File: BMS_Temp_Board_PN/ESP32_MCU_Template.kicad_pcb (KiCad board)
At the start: 2 copper layers, 195.2 x 109.5 mm, 81 parts, among them IC1 ESP32-S3-WROOM-1-N8R8, IC10 CD74HC4067PWR, IC11 CD74HC4067PWR, IC12 CD74HC4067PWR, IC13 CD74HC4067PWR, IC14 CD74HC4067PWR, IC15 CD74HC4067PWR, IC16 CD74HC4067PWR, IC17 CD74HC4067PWR, IC18 CD74HC4067PWR, IC19 CD74HC4067PWR, IC2 CP2102N-A02-GQFN28, IC20 CD74HC4067PWR, IC21 CD74HC4067PWR, IC22 CD74HC4067PWR, IC23 CD74HC4067PWR, IC24 CD74HC4067PWR, IC3 TLP175A_TPL,E, IC4 TPS2116DRLR, IC5 MIC37100-3.3WS, IC6 CD74HC4067PWR, IC7 CD74HC4067PWR, IC8 CD74HC4067PWR, IC9 CD74HC4067PWR, J1 ESP_USB, J10 B32B-PUDSS-1_LF__SN_, J11 B32B-PUDSS-1_LF__SN_, J12 B32B-PUDSS-1_LF__SN_, J13 B32B-PUDSS-1_LF__SN_, J14 B32B-PUDSS-1_LF__SN_, J15 B32B-PUDSS-1_LF__SN_, J16 B32B-PUDSS-1_LF__SN_, J17 B32B-PUDSS-1_LF__SN_, J18 B32B-PUDSS-1_LF__SN_, J19 B32B-PUDSS-1_LF__SN_, J2 B32B-PUDSS-1_LF__SN_, J20 B32B-PUDSS-1_LF__SN_, J3 B32B-PUDSS-1_LF__SN_, J4 B32B-PUDSS-1_LF__SN_, J5 B32B-PUDSS-1_LF__SN_, J6 B32B-PUDSS-1_LF__SN_, J7 B32B-PUDSS-1_LF__SN_, J8 B32B-PUDSS-1_LF__SN_, J9 B32B-PUDSS-1_LF__SN_, Q1 MMBT2222LT1G, Q2 MMBT2222LT1G, U1 USBLC6-2SC6, U2 SN65HVD230

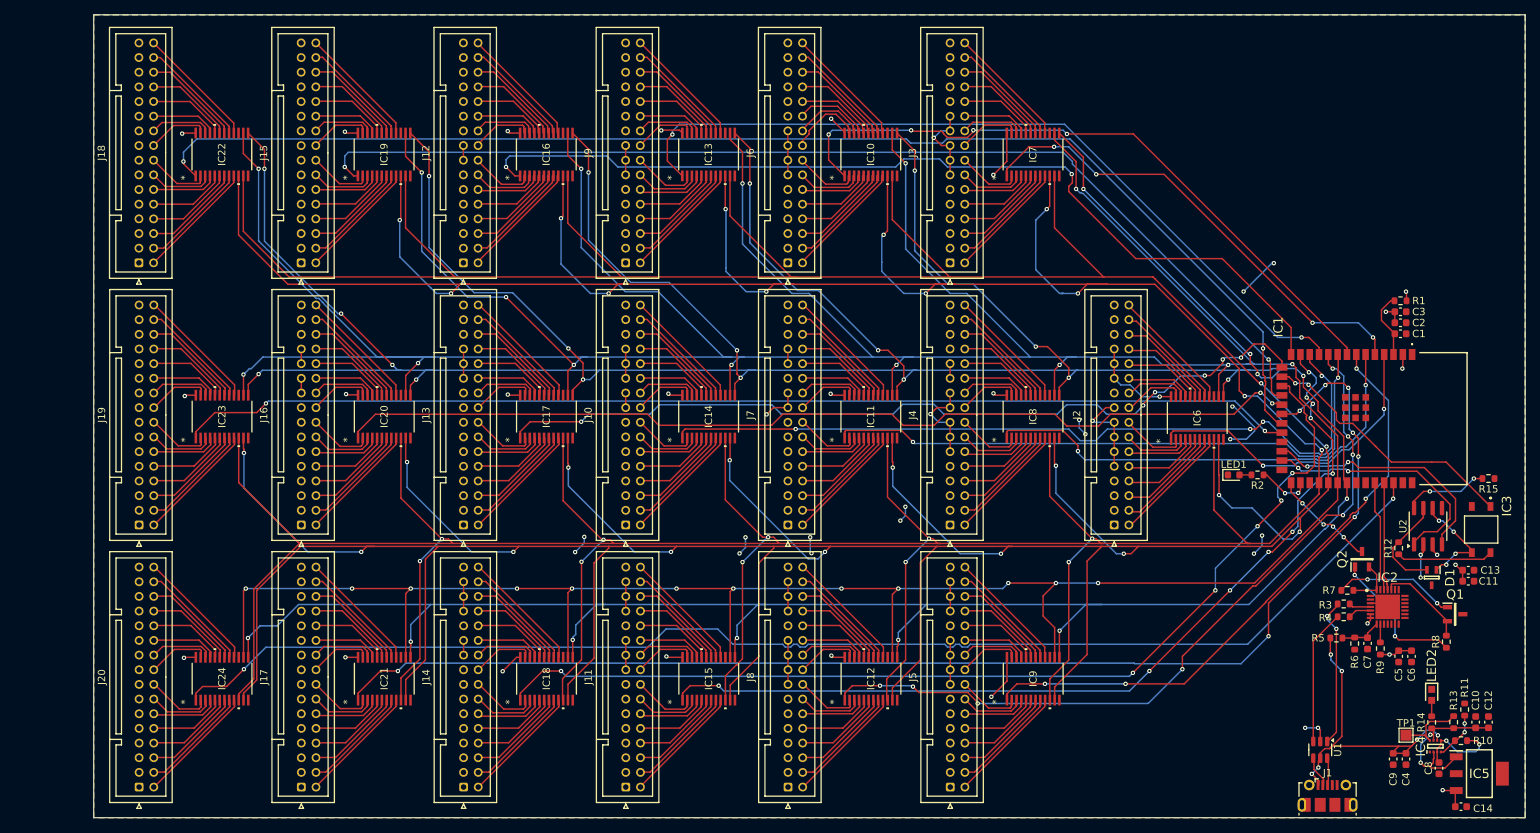
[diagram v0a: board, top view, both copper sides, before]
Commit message: Revised BMS Temperature Board and precharge circuit
the precharge circuit is a *very* basic schematic, not really finished
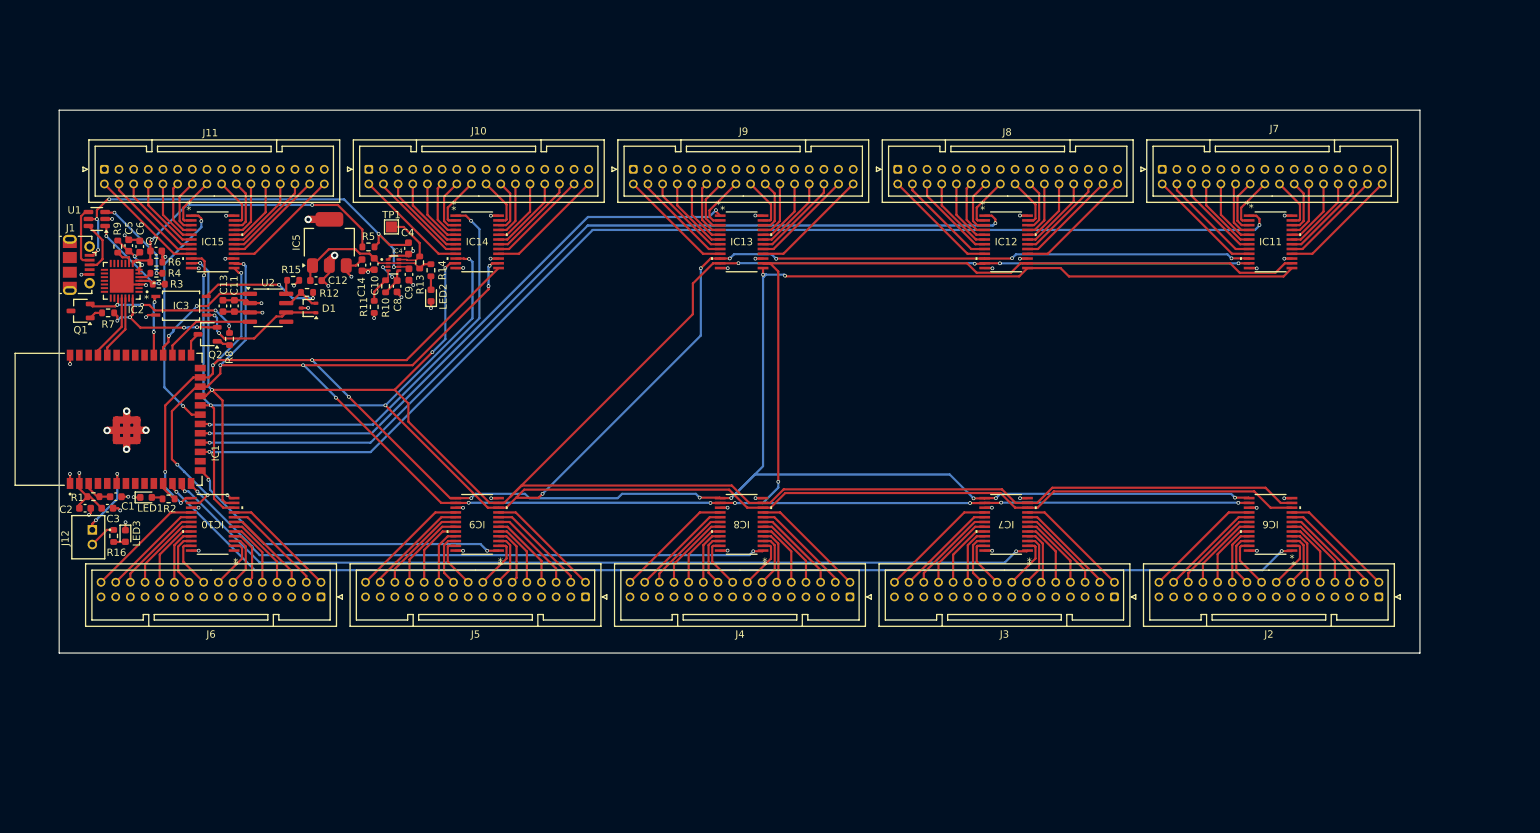
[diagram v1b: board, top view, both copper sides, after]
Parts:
- removed IC16, IC17, IC18, IC19, IC20, IC21, IC22, IC23, IC24: CD74HC4067PWR, CD74HC4067PWR:TSSOP24_4P5X7P9_TEX
- removed J13, J14, J15, J16, J17, J18, J19, J20: B32B-PUDSS-1_LF__SN_, Connector_JST:JST_PUD_B32B-PUDSS_2x16_P2.00mm_Vertical
- added LED3: LED, LED_SMD:LED_0603_1608Metric, F.Cu at (58.8, 120.8)
- added R16: 220, Resistor_SMD:R_0603_1608Metric, F.Cu at (57.2, 120.8)
- D1: footprint SDM_MiscFootprint:SOT65P210X110-3N -> Package_TO_SOT_SMD:SOT-323_SC-70
- IC1: footprint SDM_MiscFootprint:ESP32S3WROOM1N8R8 -> ESP32_S3_WROOM_1_N8R8:XCVR_ESP32S3WROOM1N8R8
- IC2: footprint SDM_MiscFootprint:QFN50P500X500X80-29N-D -> CP2102N_A02_GQFN28:QFN50P500X500X80-29N
- IC3: footprint SDM_MiscFootprint:TLP266J -> TPL175A:4pin SO6TLP17XX_TOS
- IC4: footprint SDM_MiscFootprint:SOTFL50P160X60-8L -> TPS2116DRLR:SOTFL50P160X60-8N
- IC5: footprint SDM_MiscFootprint:SOT230P700X180-4N -> Package_TO_SOT_SMD:SOT-223
- J12: value B32B-PUDSS-1_LF__SN_ -> B2B-PH-K-S; footprint Connector_JST:JST_PUD_B32B-PUDSS_2x16_P2.00mm_Vertical -> B2B_PH_K_S:JST_B2B-PH-K-S
- LED2: footprint SDM_MiscFootprint:LEDC1608X80N -> LED_SMD:LED_0603_1608Metric
- Q1, Q2: footprint SDM_MiscFootprint:SOT96P237X111-3N -> Package_TO_SOT_SMD:TSOT-23
- moved Q1 192.0 mm to (52.7, 90.1), turned to 180 degrees
- moved J1 185.1 mm to (52.5, 83.9), turned to -90 degrees
- moved C6 182.2 mm to (60.8, 81.4), turned to -90 degrees
- moved C5 182.0 mm to (59.3, 81.2), turned to 90 degrees
- moved U1 181.9 mm to (54.9, 77.6), turned to 180 degrees
- moved C2 181.2 mm to (53.3, 117.0)
- moved R9 180.7 mm to (57.8, 81.4), turned to 90 degrees
- moved R1 180.3 mm to (54.5, 115.5), turned to 0 degrees
- moved IC3 179.9 mm to (66.4, 89.4), turned to 0 degrees
- moved C3 178.4 mm to (56.4, 117.0)
- moved IC2 178.3 mm to (58.3, 86.0), turned to 180 degrees
- moved C1 176.6 mm to (57.5, 115.5)
- moved C7 173.7 mm to (63.0, 82.0), turned to 0 degrees
- moved C13 173.7 mm to (72.1, 89.5), turned to 90 degrees
- moved R7 173.2 mm to (56.5, 90.4)
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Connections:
- IC1 pad 10: /MUX7 -> unconnected-(IC1-IO17-Pad10)
- IC1 pad 11: /MUX8 -> /USER_LED
- IC1 pad 12: /MUX9 -> /MUX1
- IC1 pad 13: /MUX10 -> /MUX2
- IC1 pad 14: /MUX11 -> /MUX3
- IC1 pad 15: /MUX12 -> /MUX4
- IC1 pad 16: /CAN_TERM -> /MUX5
- IC1 pad 17: /MUX13 -> /MUX6
- IC1 pad 18: /MUX14 -> /MUX7
- IC1 pad 19: /MUX15 -> /MUX8
- IC1 pad 20: /MUX16 -> /MUX9
- IC1 pad 21: /MUX17 -> /MUX10
- IC1 pad 22: /MUX18 -> /MUX_S0
- IC1 pad 23: unconnected-(IC1-IO21-Pad23) -> /MUX_S1
- IC1 pad 24: /CAN_CTX -> /MUX_S2
- IC1 pad 25: /CAN_RTX -> /MUX_S3
- IC1 pad 28: /USER_LED -> unconnected-(IC1-IO35-Pad28)
- IC1 pad 29: unconnected-(IC1-IO36-Pad29) -> /CAN_CTX
- IC1 pad 30: /MUX_S0 -> /CAN_RTX
- IC1 pad 31: /MUX_S1 -> /CAN_TERM
- IC1 pad 32: /MUX_S2 -> unconnected-(IC1-IO39-Pad32)
- IC1 pad 33: /MUX_S3 -> unconnected-(IC1-IO40-Pad33)
- IC1 pad 38: /MUX19 -> unconnected-(IC1-IO2-Pad38)
- IC1 pad 4: /MUX1 -> unconnected-(IC1-IO4-Pad4)
- IC1 pad 5: /MUX2 -> unconnected-(IC1-IO5-Pad5)
- IC1 pad 6: /MUX3 -> /SHUTOFF
- IC1 pad 7: /MUX4 -> unconnected-(IC1-IO7-Pad7)
- IC1 pad 8: /MUX5 -> unconnected-(IC1-IO15-Pad8)
- IC1 pad 9: /MUX6 -> unconnected-(IC1-IO16-Pad9)
- J12 pad 1: +3.3V -> /SHUTOFF
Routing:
- net /MUX_S1: track 720.2 -> 336.4 mm, vias 16 -> 8
- net /MUX_S0: track 710.6 -> 345.3 mm, vias 22 -> 10
- net /MUX_S3: track 679.9 -> 332.4 mm, vias 29 -> 14
- net /MUX_S2: track 678.0 -> 334.4 mm, vias 27 -> 15
- net /MUX19: track 180.4 -> 0.00 mm, vias 2 -> 0
- net /MUX16: track 179.1 -> 0.00 mm, vias 8 -> 0
- net /MUX17: track 177.2 -> 0.00 mm, vias 2 -> 0
- net /MUX18: track 152.5 -> 0.00 mm, vias 2 -> 0
- net +3.3V: track 184.6 -> 35.5 mm, vias 31 -> 15
- net /MUX14: track 148.1 -> 0.00 mm, vias 2 -> 0
- net /MUX13: track 139.7 -> 0.00 mm, vias 6 -> 0
- net /MUX15: track 133.6 -> 0.00 mm, vias 2 -> 0
- net /MUX11: track 127.1 -> 0.00 mm, vias 2 -> 0
- net /MUX1: track 43.3 -> 159.0 mm
- net /MUX12: track 115.3 -> 0.00 mm, vias 6 -> 0
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- added copper zone on In1.Cu, net +3.3V
- added copper zone on In2.Cu, net GND
- removed copper zone on B.Cu, net +3.3V
- removed copper zone on F.Cu, net GND
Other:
- board size 195.2 x 109.5 mm -> 185.6 x 74 mm
- copper layers 2 -> 4

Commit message: (hopefully) final revision of the bms temp board
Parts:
- added H1: MountingHole, MountingHole:MountingHole_2.2mm_M2, F.Cu at (235.4, 65.8)
- added H2: MountingHole, MountingHole:MountingHole_2.2mm_M2, F.Cu at (235.4, 133.4)
- added H3: MountingHole, MountingHole:MountingHole_2.2mm_M2, F.Cu at (50.5, 133.4)
- added H4: MountingHole, MountingHole:MountingHole_2.2mm_M2, F.Cu at (50.5, 65.8)
- added J13: SM04B-ULHK-1TA1-ETB_HF_, SM04B-ULH:SM04BULHK1TA1ETBHF, F.Cu at (230.8, 97.7)
- J10, J11, J2, J3, J4, J5, J6, J7, J8, J9: footprint Connector_JST:JST_PUD_B32B-PUDSS_2x16_P2.00mm_Vertical -> ESP32_S3_WROOM_1_N8R8:JST_PUD_B32B-PUDSS_2x16_P2.00mm_Vertical_PN
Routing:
- net /CAN+: track 5.26 -> 211.6 mm, vias 0 -> 2
- net /CAN-: track 18.8 -> 225.1 mm, vias 2 -> 4
- net +5V: track 20.6 -> 161.1 mm, vias 0 -> 2
- net /MUX5: track 0.00 -> 15.3 mm
- net /MUX_S1: track 336.4 -> 345.9 mm
- net GND: track 89.5 -> 91.2 mm, vias 49 -> 50
- net /MUX_S2: track 334.4 -> 333.8 mm
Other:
- board size 185.6 x 74 mm -> 190.5 x 74.1 mm

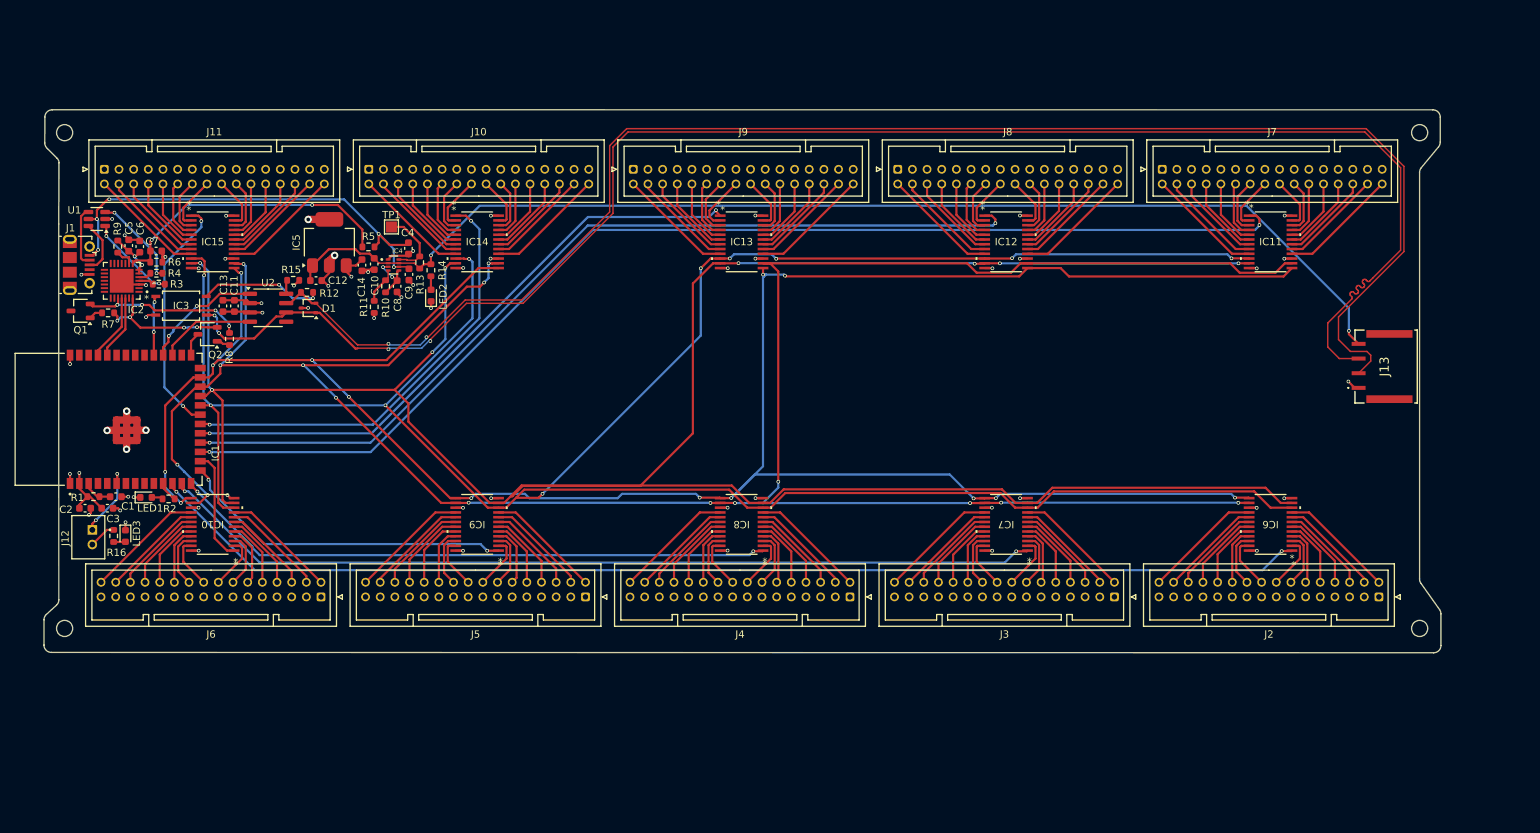
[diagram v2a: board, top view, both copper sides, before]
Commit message: Reviewing Board
Ready for DAQ Review
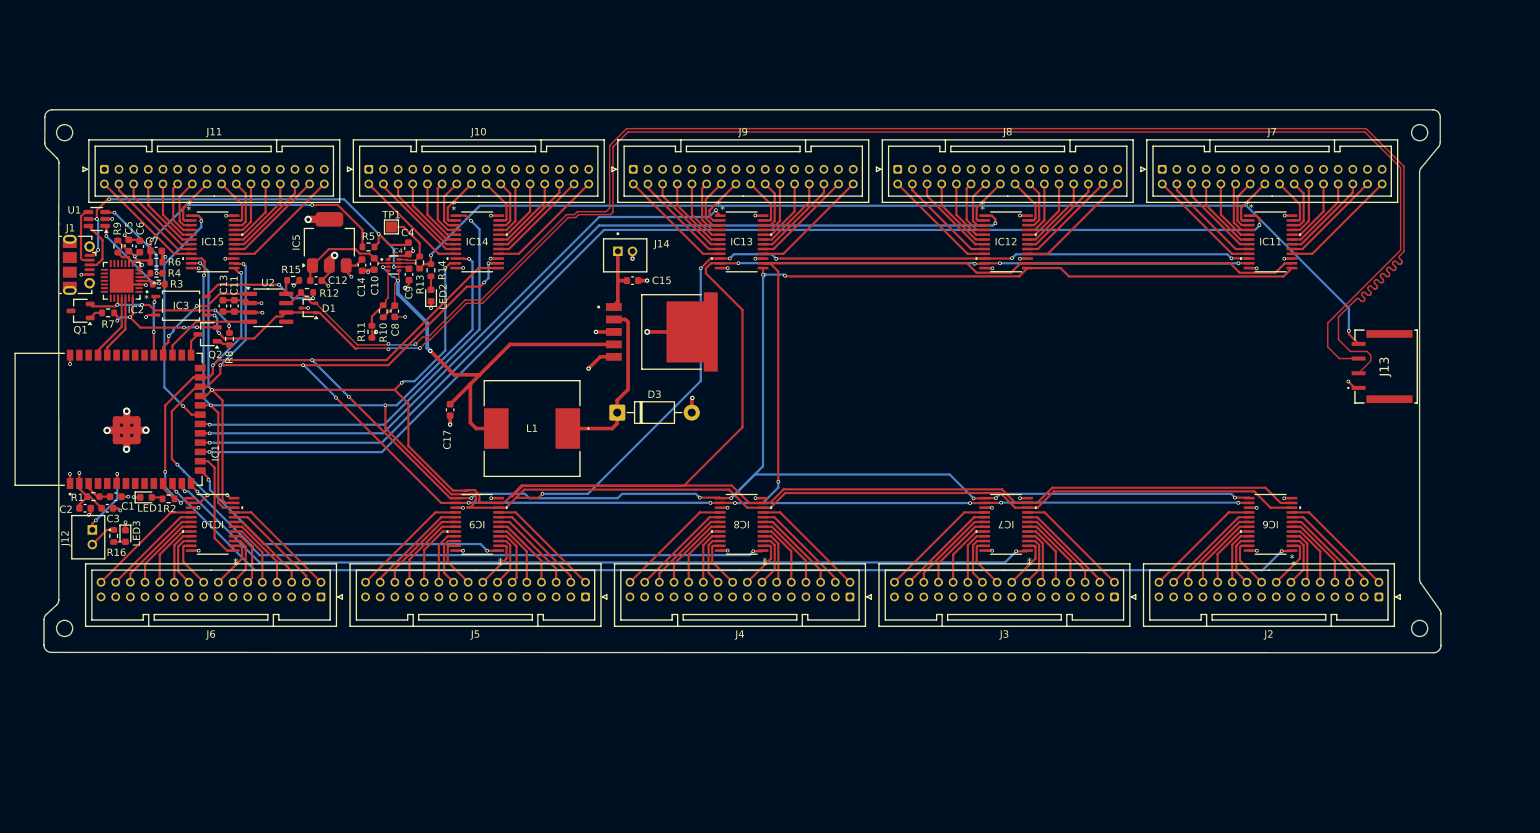
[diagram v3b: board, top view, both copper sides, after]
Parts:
- added C15: 100uF, Capacitor_SMD:C_0603_1608Metric, F.Cu at (128.0, 86.0)
- added C17: 330uF, Capacitor_SMD:C_0603_1608Metric, F.Cu at (103.1, 103.6)
- added D3: 1N5819, Diode_THT:D_DO-41_SOD81_P10.16mm_Horizontal, F.Cu at (125.9, 104.0)
- added J14: B2B-PH-K-S, B2B_PH_K_S:JST_B2B-PH-K-S, F.Cu at (127.0, 82.5)
- added L1: 330uH, Nadine:IND_SPD127R_API, F.Cu at (114.3, 106.2)
- added U3: LM2575HVS-5.0_NOPB, Nadine:VREG_LM2575HVS-5.0_NOPB, F.Cu at (132.0, 93.0)
- moved C8 3.42 mm to (95.6, 90.2)
- moved R10 3.42 mm to (94.0, 90.2)
- moved R11 3.42 mm to (92.5, 93.0)
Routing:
- net VCC: track 7.17 -> 65.1 mm, vias 2 -> 3
- net GND: track 91.2 -> 116.5 mm, vias 50 -> 57
- net Net-(D3-K): track 0.00 -> 23.5 mm
- net /MUX_S1: track 345.9 -> 357.5 mm
- net /CAN+: track 211.6 -> 220.9 mm
- net /MUX_S0: track 345.3 -> 354.5 mm
- net +12V: track 0.00 -> 9.12 mm
- net Net-(IC4-PR1): track 4.93 -> 8.46 mm
- net /CAN-: track 225.1 -> 221.8 mm
- net /MUX9: track 60.3 -> 61.2 mm
